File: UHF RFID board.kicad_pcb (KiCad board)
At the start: 2 copper layers, 67.3 x 36.7 mm, 24 parts, among them J1 FZ_full_module, J10 SIM_Card, J2 picoblade, J3 Conn_02x04_Odd_Even, J4 Conn_02x05_Odd_Even, SW1 SW_SPDT, U1 YRM1001, U2 SEC1210

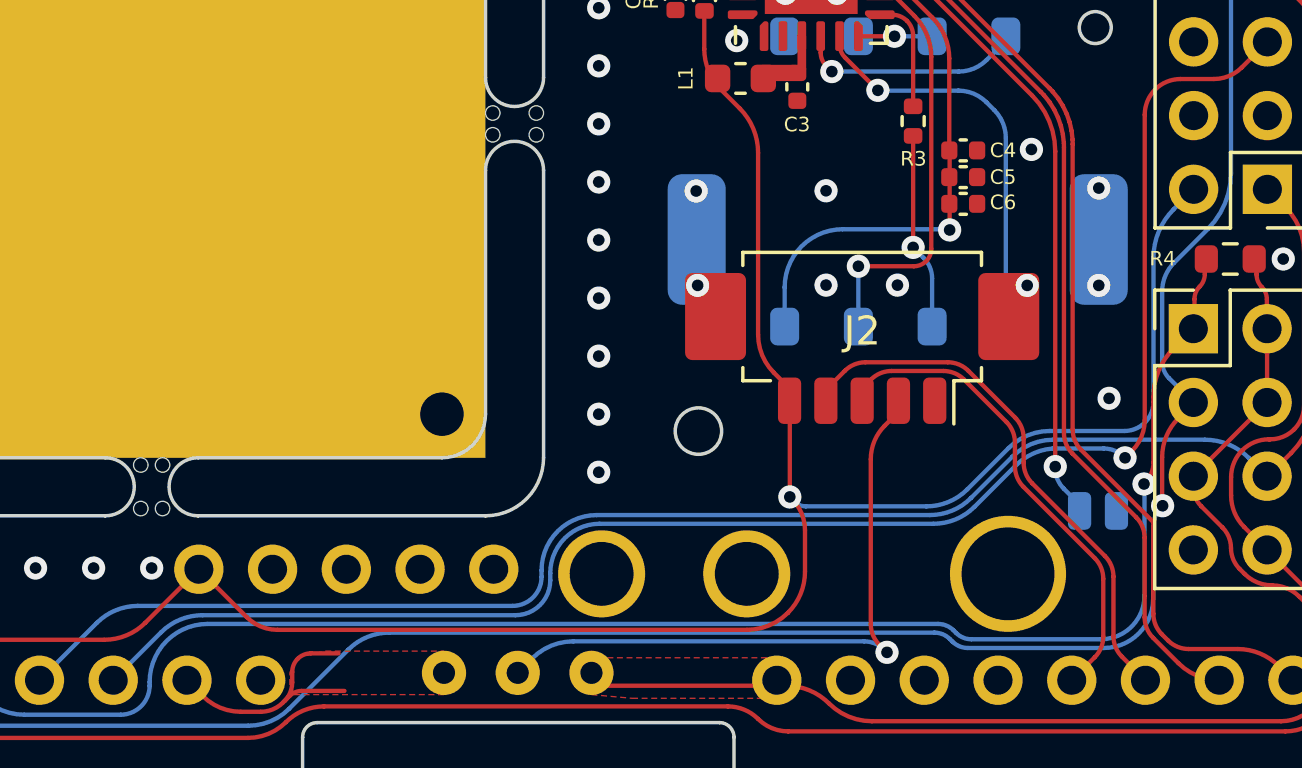
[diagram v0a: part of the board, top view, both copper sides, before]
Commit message: changed the footprint for SIM card to the correct one
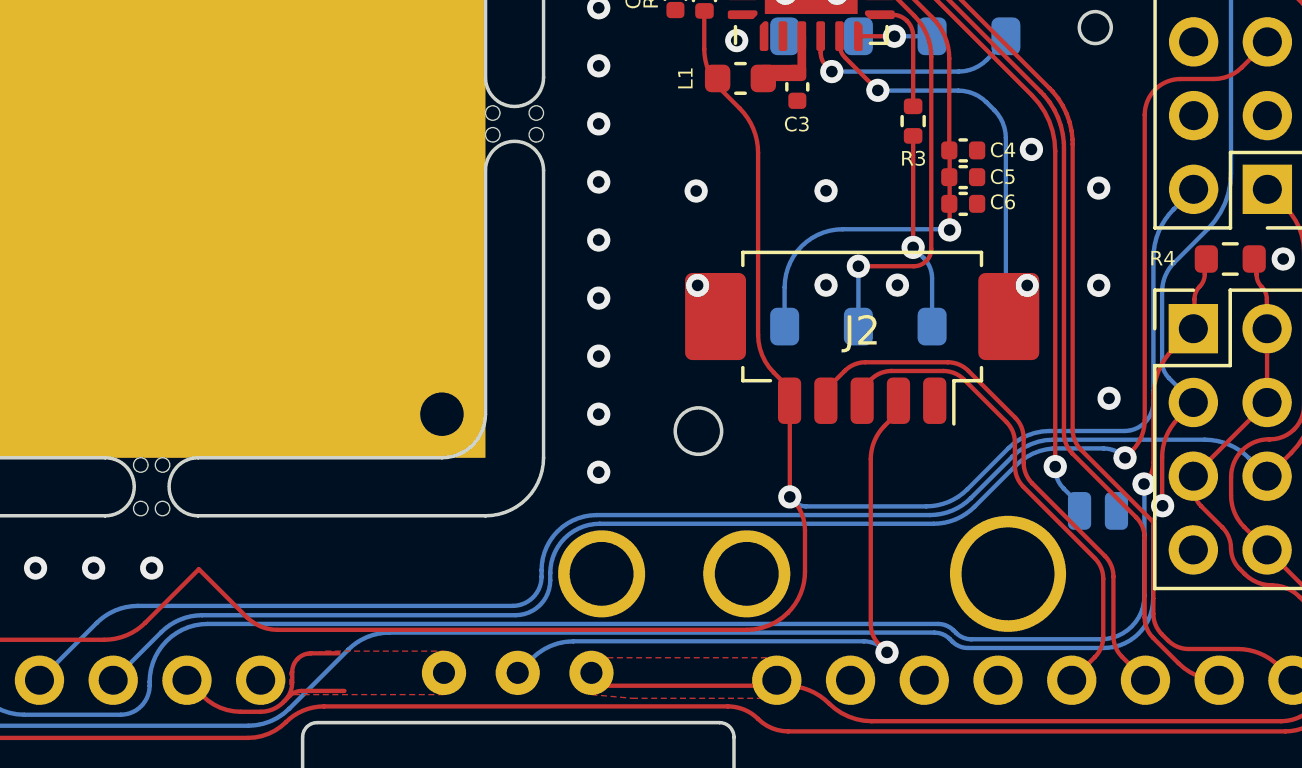
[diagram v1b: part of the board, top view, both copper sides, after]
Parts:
- J10: footprint nard_sam:115c-bc00 sim simcard card connector -> Custom footprints:SIMMP-00801B000-G sim card connector
- U1: footprint RFID_NFC_footprints:UHF_RFID_35x35_YRM1001_module_through-board with mounting holes 35-40-50 -> RFID_NFC_footprints:UHF_RFID_35x35_YRM1001_module_through-board no_header with mounting holes 35-40-50
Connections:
- net Net-(J1B-3V3) renamed +3.3V
- net Net-(J2-Pin_2) renamed /EN

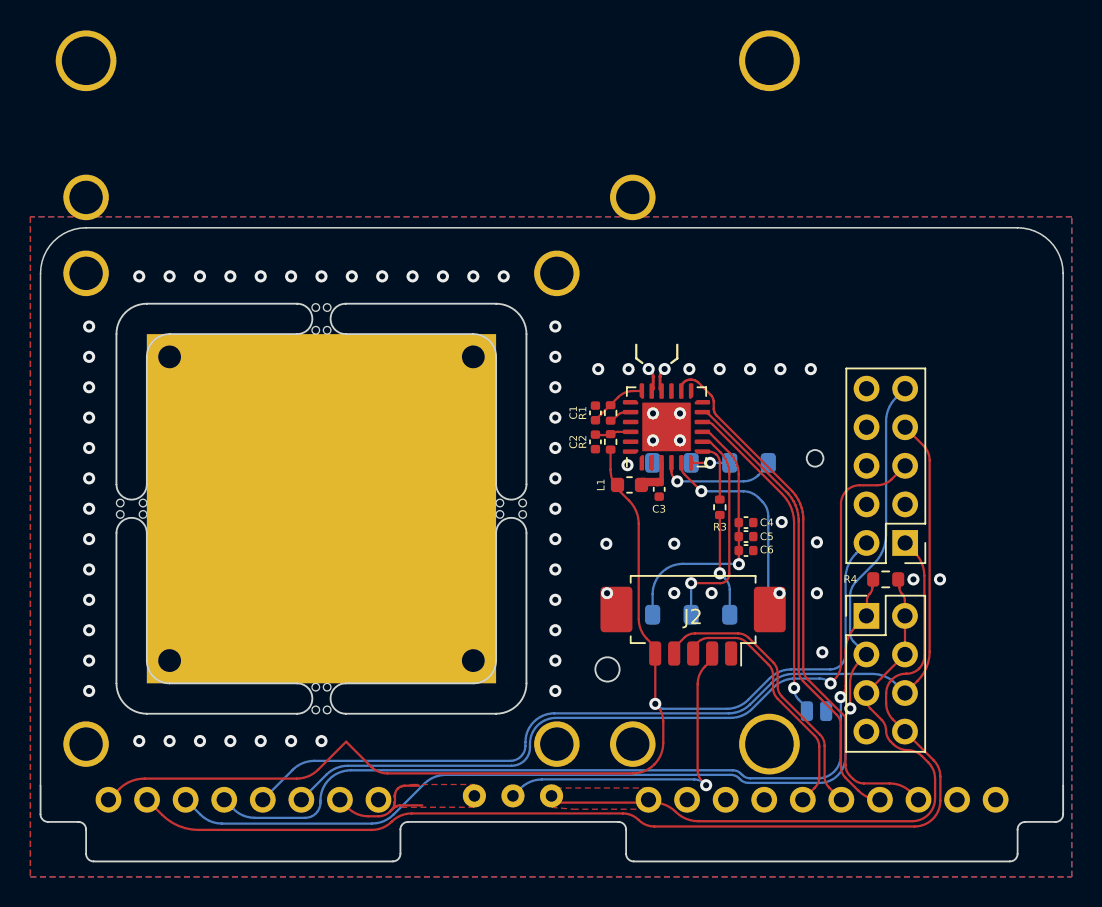
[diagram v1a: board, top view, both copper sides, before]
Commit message: Add files via upload
updated board version to 1.2:
- changed ICSP from 10 pin header to 6 pin header. 10 pin ICSP connections can be done with a 6 to 10 pin adapter cable.
- changed name on board to UHF | RFID | SAM, removing '1/2 nard' from the name for clarity on what the board is and does.
- removed header that was meant to hard-connect the UHF module to the board: it is not used for communication with the board after all. 
- updated the QR codes designs for better machine readability
- various routing improvements.

schematics:
- changed ICSP from 10 pin header to 6 pin header

other:
reverse-engineered the YRM1001 and YRM200 boards to have them in Kicad. Measurements should be close enough for OKing designs using those modules.
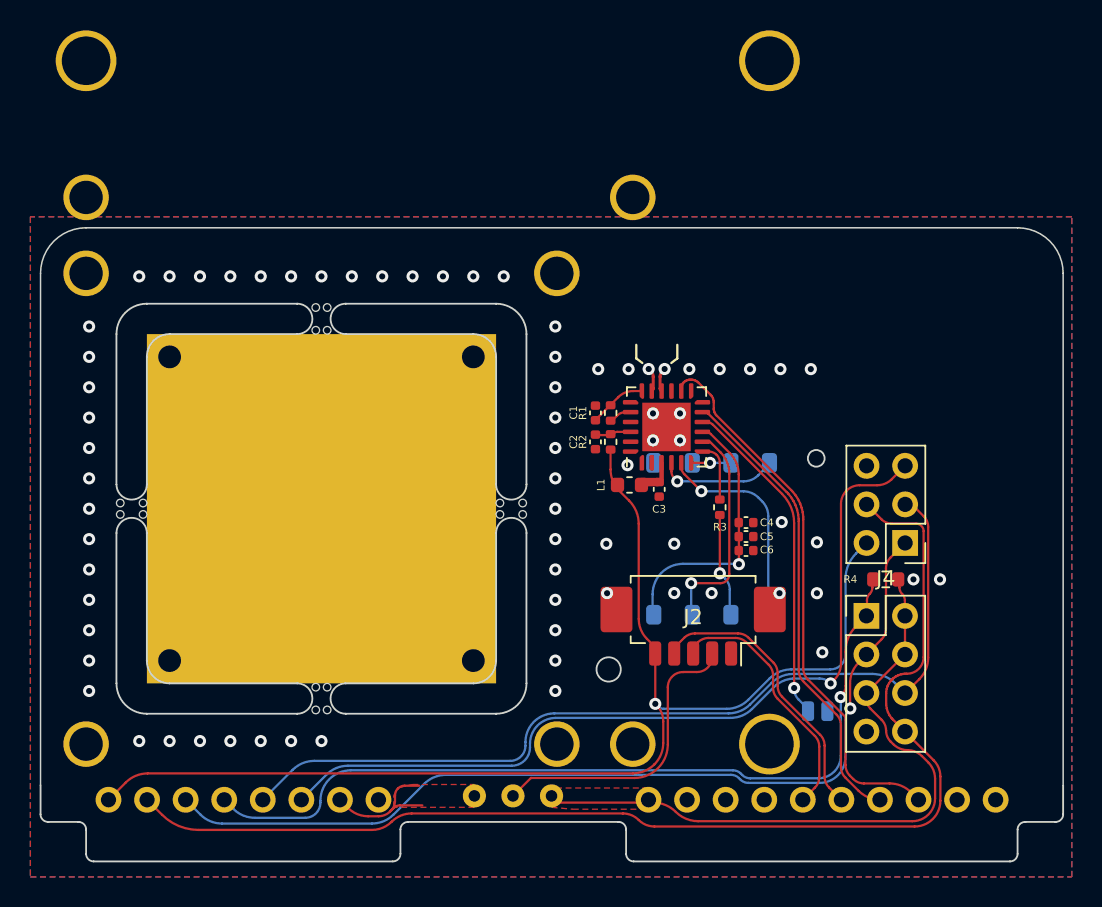
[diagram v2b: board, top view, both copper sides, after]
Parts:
- J4: value Conn_02x05_Odd_Even -> Conn_02x03_Odd_Even; footprint Connector_PinHeader_2.54mm:PinHeader_2x05_P2.54mm_Vertical -> Connector_PinHeader_2.54mm:PinHeader_2x03_P2.54mm_Vertical
- moved J10 0.08 mm to (158.8, 121.1)
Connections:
- J4 pad 1: MOSI -> MISO
- J4 pad 3: unconnected-(J4-Pin_3-Pad3) -> CLK
- J4 pad 4: GND -> MOSI
- U2 pad 1: unconnected-(U2-SC2_RST_N-Pad1) -> /SC2_RST
- U2 pad 2: unconnected-(U2-SC2_VCC-Pad2) -> /SC2_VCC
- U2 pad 21: unconnected-(U2-SC2_PRSNT_N/JTAG_TDI-Pad21) -> /SC2_PRsNT
- U2 pad 23: unconnected-(U2-SC2_IO-Pad23) -> /SC2_IO
- U2 pad 24: unconnected-(U2-SC2_CLK-Pad24) -> Net-(U2-SC2_CLK)
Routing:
- net MISO: track 72.5 -> 61.7 mm
- net CLK: track 65.0 -> 60.1 mm
- net MOSI: track 74.7 -> 79.3 mm
- net /EN: track 22.3 -> 19.8 mm, vias 1 -> 0
- net +5V: track 82.0 -> 80.5 mm
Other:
- board text added: "UHF | RFID | SAM Version 1.2"
- board text removed: "UHF | RFID | ½NARD board Version 1.1"

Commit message: Version 2.0 RELEASE
- removed M3 support hole for 50x50 modules: there was only one M3 hole anyway, so no good mechanical support. case for the board can designed with mounting holes for that size module if need be.
- added second SAM slot as per SEC1210 datasheet.
- rerouted the vast majority of the board to accommodate all the changes.
- changed board thickness to 1.2 from 1.6 as per Flipper Zero module specs
- repositioned the SAM slots close to the board edge for ease of access to the SAMs with a case on.
- repositioned all of the components needed for the SEC1210 for addition of second SAM slot
- repositioned Picoblade connector for addition of second SAM slot
- repositioned ICSP and ISP headers for addition of second SAM slot
- updated legend to V2.0
- added GND and +5V vias near the usb connection for the SEC1210 in case they are needed.
- removed the selection switch and replaced it with a solder jumper. switch was overkill and this feature is there 'just in case': the YRM1001 does *NOT* have the enable pin actually routed on the module. It can be done but it requires desoldering the daughterboard from the module, cutting traces, and putting in bodge wires.
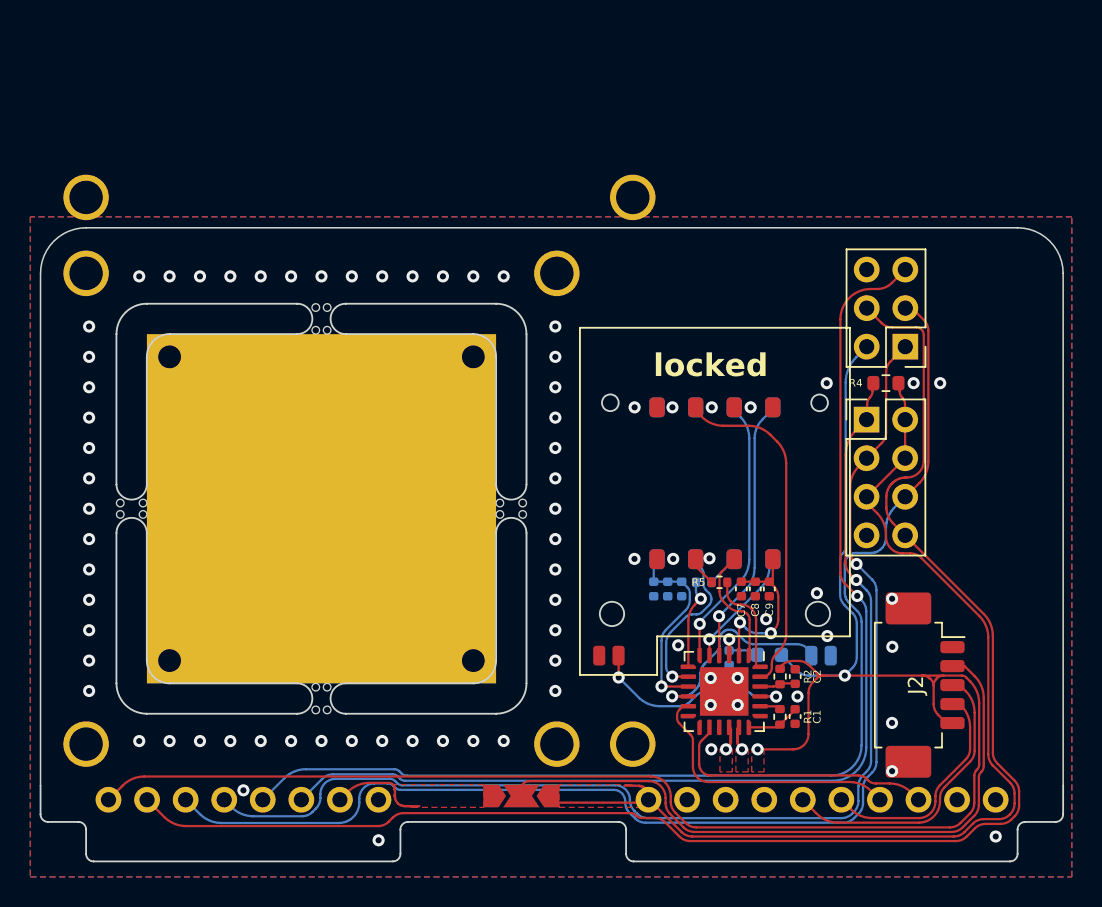
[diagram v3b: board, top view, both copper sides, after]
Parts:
- removed SW1: SW_SPDT, Custom footprints:1K2 09.03201.02 SECME
- added C7: 10uF, Capacitor_SMD:C_0402_1005Metric, F.Cu at (164.5, 119.4)
- added C8: 1uF, Capacitor_SMD:C_0402_1005Metric, F.Cu at (165.4, 119.4)
- added C9: 0.1uF, Capacitor_SMD:C_0402_1005Metric, F.Cu at (166.4, 119.4)
- added J11: SIM_Card, Custom footprints:SIMMP-00801B000-G sim card connector, F.Cu at (166.6, 117.4)
- added JP1: SolderJumper_3_Open, Jumper:SolderJumper-3_P2.0mm_Open_TrianglePad1.0x1.5mm, F.Cu at (150.0, 133.0)
- added R5: 43R, Resistor_SMD:R_0402_1005Metric, F.Cu at (163.1, 118.9)
- C3, C4, C5, C6, L1, R3: moved to B.Cu
- U1: footprint RFID_NFC_footprints:UHF_RFID_35x35_YRM1001_module_through-board no_header with mounting holes 35-40-50 -> RFID_NFC_footprints:UHF_RFID_35x35_YRM1001_module_through-board no_header with mounting holes 35-40
- moved C1 23.9 mm to (168.1, 127.8), turned to -90 degrees
- moved R1 22.9 mm to (167.1, 127.8), turned to -90 degrees
- moved C2 20.3 mm to (168.1, 125.1), turned to 90 degrees
- moved R2 19.1 mm to (167.1, 125.1), turned to -90 degrees
- moved U2 17.8 mm to (163.4, 126.1), turned to -90 degrees
- moved J2 15.3 mm to (176.0, 125.7), turned to -90 degrees
- moved L1 14.5 mm to (166.4, 123.7), turned to 180 degrees
- moved J3 12.9 mm to (172.8, 108.2)
- moved J4 12.9 mm to (175.3, 103.4)
- moved R4 12.9 mm to (174.0, 105.8)
- moved C3 12.0 mm to (163.7, 123.9)
- moved C6 6.58 mm to (158.8, 119.4), turned to -90 degrees
- moved C5 6.20 mm to (159.7, 119.4), turned to -90 degrees
- moved C4 6.09 mm to (160.6, 119.4), turned to -90 degrees
- moved R3 5.05 mm to (162.0, 118.9), turned to 0 degrees
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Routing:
- net +5V: track 80.5 -> 123.2 mm, vias 1 -> 2
- net /EN: track 19.8 -> 44.1 mm
- net +3.3V: track 44.5 -> 68.2 mm
- net /SC2_IO: track 0.00 -> 22.8 mm
- net MOSI: track 79.3 -> 100.2 mm
- net MISO: track 61.7 -> 80.9 mm
- net CS: track 55.8 -> 74.3 mm
- net /PC0: track 36.5 -> 18.0 mm
- net RST: track 55.9 -> 73.7 mm
- net /SC1_IO: track 2.54 -> 18.0 mm
- net CLK: track 60.1 -> 74.3 mm
- net /SC2_PRsNT: track 0.00 -> 14.0 mm, vias 0 -> 2
- net /PC1: track 30.7 -> 18.1 mm
- net /SC2_VCC: track 0.00 -> 11.6 mm, vias 0 -> 2
- net /SC1_C8: track 7.86 -> 17.6 mm
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- added copper zone on F.Cu, net +5V
- added copper zone on F.Cu, net /USB_DN
- added copper zone on F.Cu, net /USB_DP
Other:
- board text added: "+5V"
- board text added: "GND"
- board text added: "UHF | RFID | SAM Version 2.O"
- board text added: "locked"
- board text removed: "UHF | RFID | SAM Version 1.2"
- board text removed: "card 1"

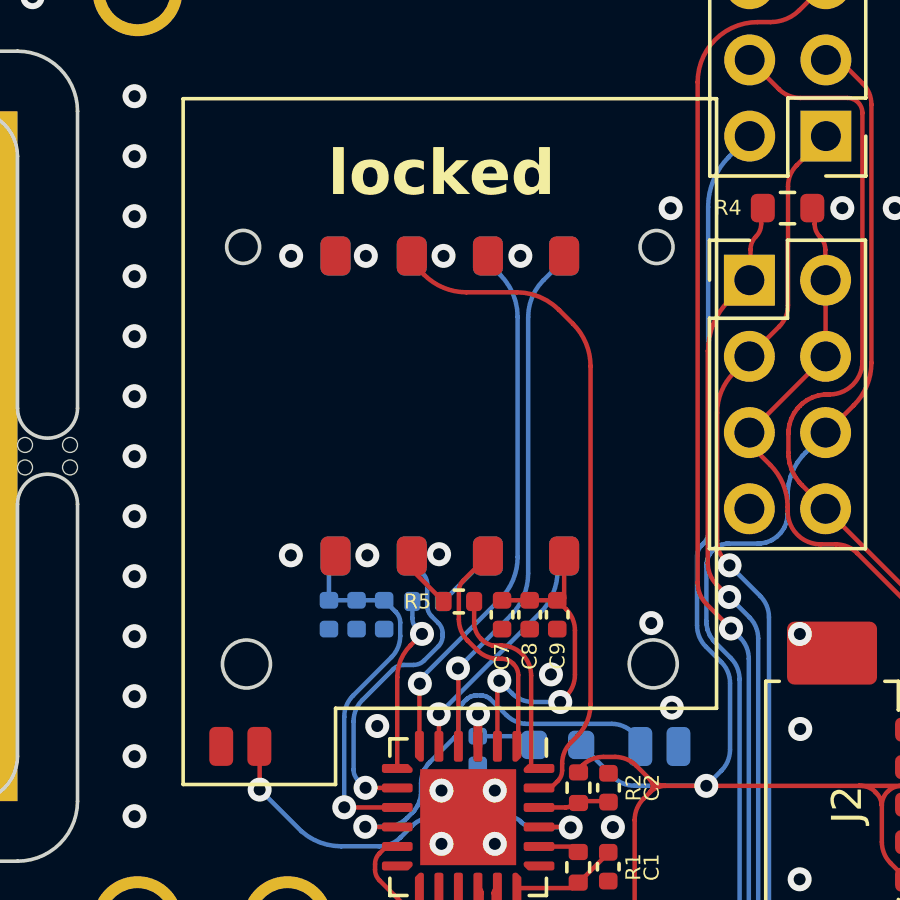
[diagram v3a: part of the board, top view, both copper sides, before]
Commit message: finalization for V2.0 board production aspect
- specified adhesive layers for all the back-mounted components
- added footprint and model for kapton tape over USB breakout vias
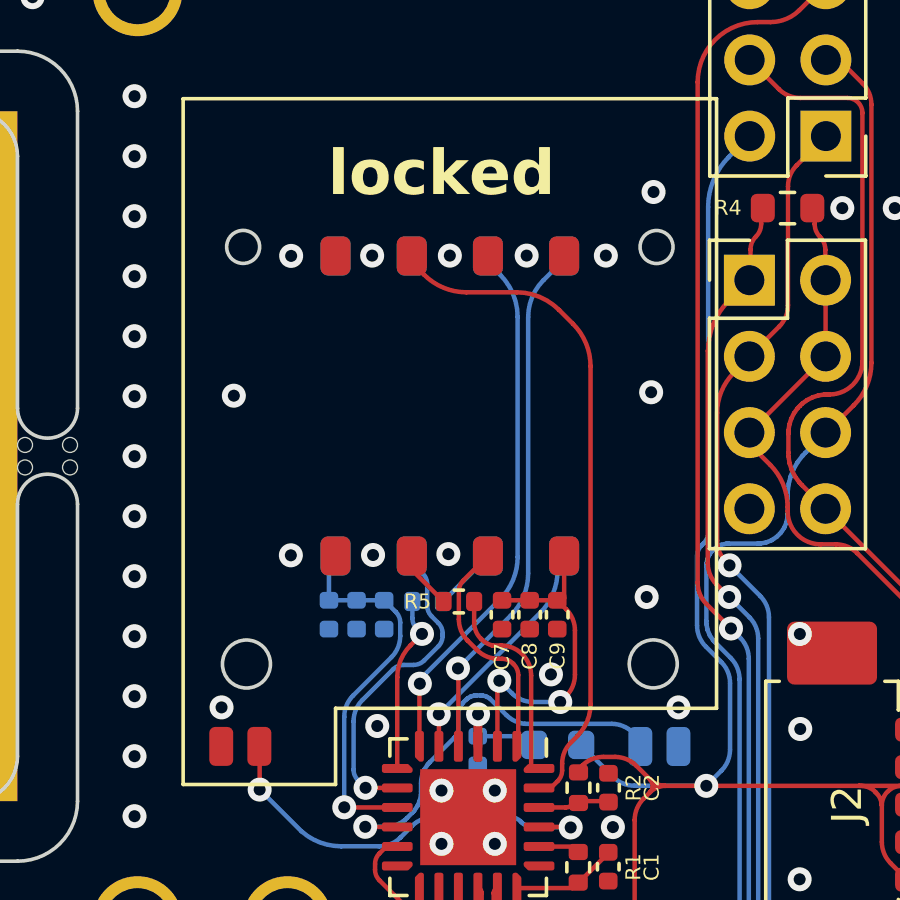
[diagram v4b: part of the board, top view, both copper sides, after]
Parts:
- added REF**: kapton tape 5x3, custom misc:kapton tape 5x3, F.Cu at (164.1, 130.7)
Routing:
- net GND: vias 79 -> 83
